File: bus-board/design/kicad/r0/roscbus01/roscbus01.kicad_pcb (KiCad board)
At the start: 2 copper layers, 160.1 x 115.9 mm, 42 parts, among them J1 Conn_01x03_Male, J2 Screw_Terminal_01x02, J3 Jack-DC, J4 USB_B_Micro, SW1 POWER, U1 L7805

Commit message: Updates and add CAM outputs
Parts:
- moved REF** 27.5 mm to (115.8, 136.5)
- moved OSHW_Mono_0.25_Scale 5.55 mm to (115.8, 81.5)
- moved C5 4.09 mm to (118.3, 41.4)
- moved BUS1-2 3.36 mm to (106.1, 142.1)
- moved BUS2-2 3.36 mm to (135.3, 142.1)
- moved BUS3-2 3.36 mm to (164.5, 142.1)
- moved BUS4-2 3.36 mm to (193.7, 142.1)
- moved JBUS5-2 3.36 mm to (223.0, 142.1)
- moved BUS1-1 2.12 mm to (106.1, 55.4)
- moved BUS2-1 2.12 mm to (135.3, 55.4)
- moved BUS3-1 2.12 mm to (164.5, 55.4)
- moved BUS4-1 2.12 mm to (193.7, 55.4)
- moved BUS5-1 2.12 mm to (223.0, 55.4)
- moved C2 2.12 mm to (209.8, 41.4)
- moved C3 2.12 mm to (179.7, 41.4)
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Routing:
- net VCC: track 164.0 -> 160.5 mm
- net Net-(J1-Pad2): track 21.5 -> 22.8 mm
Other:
- board text added: "3-4 - 9-18VDC*"
- board text added: "D+"
- board text added: "D-"
- board text added: "ID"
- board text removed: "3-4 - 9-20VDC*"

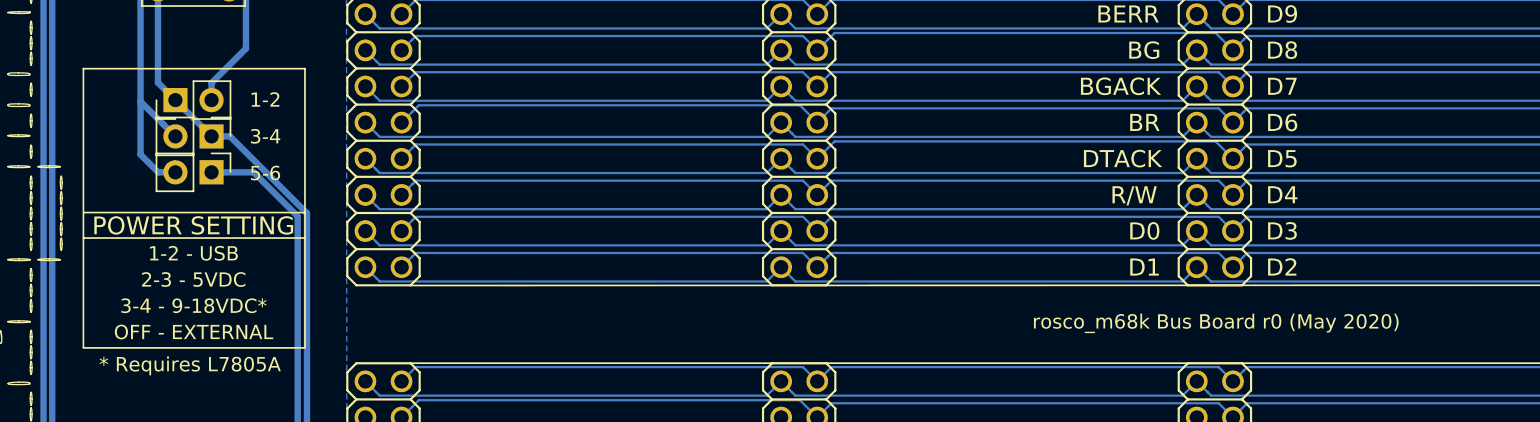
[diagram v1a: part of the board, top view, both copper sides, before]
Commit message: Silkscreen fixes
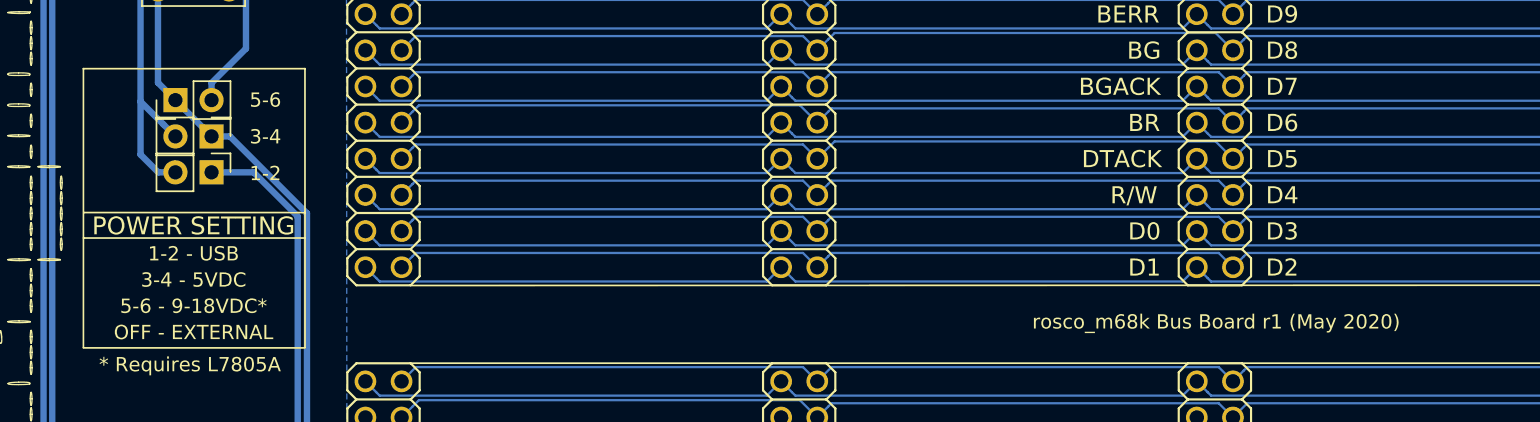
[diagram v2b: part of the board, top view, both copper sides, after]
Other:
- board text added: "3-4 - 5VDC"
- board text added: "5-6 - 9-18VDC*"
- board text added: "rosco_m68k Bus Board r1 (May 2020)"
- board text removed: "2-3 - 5VDC"
- board text removed: "3-4 - 9-18VDC*"
- board text removed: "rosco_m68k Bus Board r0 (May 2020)"
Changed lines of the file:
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@@
     (effects (font (size 1.5 1.5) (thickness 0.15)))
   )
-  (gr_text "rosco_m68k Bus Board r0 (May 2020)" (at 159.55 123.975) (layer F.SilkS)
+  (gr_text "rosco_m68k Bus Board r1 (May 2020)" (at 159.55 123.975) (layer F.SilkS)
     (effects (font (size 1 1) (thickness 0.15)))
   )
@@
     (effects (font (size 1 1) (thickness 0.15)))
   )
-  (gr_text 5-6 (at 92.74 113.55) (layer F.SilkS)
+  (gr_text 1-2 (at 92.74 113.55) (layer F.SilkS)
     (effects (font (size 1 1) (thickness 0.15)))
   )
@@
     (effects (font (size 1 1) (thickness 0.15)))
   )
-  (gr_text 1-2 (at 92.74 108.39) (layer F.SilkS)
+  (gr_text 5-6 (at 92.74 108.39) (layer F.SilkS)
     (effects (font (size 1 1) (thickness 0.15)))
   )
@@
   (gr_line (start 95.52 106.18) (end 79.95 106.18) (layer F.SilkS) (width 0.12))
   (gr_line (start 95.52 125.76) (end 95.52 106.18) (layer F.SilkS) (width 0.12))
-  (gr_text "3-4 - 9-18VDC*" (at 87.69 122.876666) (layer F.SilkS)
+  (gr_text "5-6 - 9-18VDC*" (at 87.69 122.876666) (layer F.SilkS)
     (effects (font (size 1 1) (thickness 0.15)))
   )
-  (gr_text "2-3 - 5VDC" (at 87.69 121.033333) (layer F.SilkS)
+  (gr_text "3-4 - 5VDC" (at 87.69 121.033333) (layer F.SilkS)
     (effects (font (size 1 1) (thickness 0.15)))
   )

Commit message: Minor fixes
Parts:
- removed the REF** at (115.8, 136.5)
- moved REF** 6.84 mm to (70.8, 119.0), turned to 270 degrees
- moved D1 6.22 mm to (82.4, 68.6)
- moved C8 4.63 mm to (86.4, 76.2), turned to 90 degrees
- moved U1 4.30 mm to (87.2, 80.2)
- moved C7 3.68 mm to (82.2, 102.8)
- moved JP4 3.00 mm to (86.0, 113.5)
- moved JP5 3.00 mm to (86.0, 110.9)
- moved JP6 3.00 mm to (83.4, 108.4)
- moved C1 2.27 mm to (87.0, 62.6)
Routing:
- net Net-(C8-Pad1): track 52.1 -> 44.2 mm
- net VCC: track 160.5 -> 162.5 mm
- net Net-(C7-Pad1): track 59.8 -> 61.4 mm
- net Net-(JP6-Pad2): track 32.7 -> 32.0 mm
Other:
- board text added: "- +"
- board text added: "5-6 - 9-12VDC*"
- board text added: "Center Positive"
- board text removed: "5-6 - 9-18VDC*"
- board text removed: "Read Manual Before Connecting Power!"

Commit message: Fix #8
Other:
- board text added: "+ -"
- board text removed: "- +"
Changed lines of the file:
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@@
   )
   (setup
-    (last_trace_width 0.45)
+    (last_trace_width 0.16)
     (user_trace_width 0.45)
     (trace_clearance 0.16)
@@
       (net 63 VCC) (solder_mask_margin 0.1016))
   )
-  (gr_text "-   +" (at 69.8 61.620001 90) (layer F.SilkS)
+  (gr_text "+   -" (at 69.8 61.620001 90) (layer F.SilkS)
     (effects (font (size 1 1) (thickness 0.15)))
   )

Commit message: Fix #7
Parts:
- H1, H2, H3, H4, H5, H6, H7, H8: footprint MountingHole:MountingHole_2.7mm_M2.5 -> MountingHole:MountingHole_3.2mm_M3
- R1: value 330R -> 1K
- moved C5 0.73 mm to (117.6, 41.4)
- moved H5 0.63 mm to (224.9, 147.4)
- moved H6 0.63 mm to (174.3, 147.4)
- moved H7 0.63 mm to (122.3, 147.4)
- moved H8 0.63 mm to (72.4, 147.4)
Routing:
- net EXT15: track 120.3 -> 121.0 mm
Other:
- board text added: "rosco_m68k Bus Board r2 (June 2020)"
- board text removed: "rosco_m68k Bus Board r1 (May 2020)"

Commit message: Bus revision 3
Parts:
- removed D1: BAT43, Diode_THT:D_DO-35_SOD27_P7.62mm_Horizontal
- moved C7 1.90 mm to (82.2, 104.7)
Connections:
- C8 pad 1: Net-(C8-Pad1) -> VCC
- JP4 pad 2: Net-(C8-Pad1) -> VCC
- JP5 pad 2: Net-(C8-Pad1) -> VCC
- U1 pad 3: Net-(C8-Pad1) -> VCC
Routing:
- net VCC: track 162.5 -> 216.3 mm
- net Net-(C8-Pad1): track 44.2 -> 0.00 mm
- net Net-(C7-Pad1): track 61.4 -> 59.5 mm
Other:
- board text added: "rosco_m68k Bus Board r3 (August 2020)"
- board text removed: "rosco_m68k Bus Board r2 (June 2020)"
